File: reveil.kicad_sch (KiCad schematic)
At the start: 18 parts, among them J1 Barrel_Jack_Switch, J2 AudioJack3_SwitchTR, M1 Motor_DC, Q1 2N3904, Q2 IRF540N

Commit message: Corrige le pinout du footprint du switch ALARME_ON_OFF1 (court-circuit GND/+3V3)
Le footprint système Button_Switch_THT:SW_Slide-03_Wuerth-WS-SLTV a
les pads 1 et 2 physiquement inversés par rapport au composant monté
(pin 1 attendu à gauche, pin 2 au centre — le footprint avait
l'inverse). Résultat : selon la position du switch, +3V3 et GND se
retrouvaient court-circuités via l'interrupteur, faisant chauffer le
Pico et les câbles d'alimentation.

Correctif : nouvelle librairie locale reveil.pretty/ avec une copie
du footprint où seuls les pads 1 et 2 échangent leur géométrie (même
taille/forme/perçage, juste la position), enregistrée via
fp-lib-table. Le schéma (ALARME_ON_OFF1) et le PCB référencent
maintenant reveil:SW_Slide-03_... ; les pistes ont été reroutées en
conséquence.

Confirmé par :
- Mesure au multimètre (court quasi 0 Ω entre GND et +3V3, reproduit
  en rebranchant ces deux fils) ayant permis d'identifier la cause
- ERC propre (0 erreur/avertissement)
- DRC propre après routage (plus de shorting_items ni de pad non
  connecté sur ALARME_ON_OFF1)

Co-Authored-By: Claude Sonnet 5 <noreply@anthropic.com>
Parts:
- ALARME_ON_OFF1: footprint Button_Switch_THT:SW_Slide-03_Wuerth-WS-SLTV_10x2.5x6.4_P2.54mm -> reveil:SW_Slide-03_Wuerth-WS-SLTV_10x2.5x6.4_P2.54mm
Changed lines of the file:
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@@
 			)
 		)
-		(property "Footprint" "Button_Switch_THT:SW_Slide-03_Wuerth-WS-SLTV_10x2.5x6.4_P2.54mm"
+		(property "Footprint" "reveil:SW_Slide-03_Wuerth-WS-SLTV_10x2.5x6.4_P2.54mm"
 			(at 91.44 144.78 0)
 			(effects

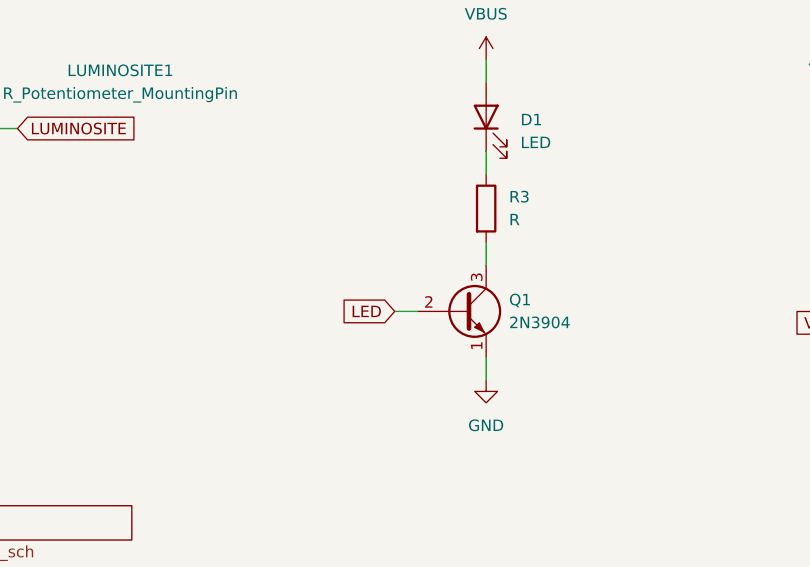
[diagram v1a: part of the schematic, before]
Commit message: Ajoute R4 (résistance de base) et corrige R3 pour le circuit LED D1
GP17 pilotait directement la base de Q1 sans résistance série : la
broche ne pouvait pas atteindre un état haut propre (chargée par la
jonction base-émetteur, ~0.6-0.7V), maintenant Q1 en conduction
partielle constante au lieu de commuter — la LED restait allumée en
continu, faiblement, au lieu de clignoter.

- R4 = 1.5 kΩ ajoutée en série entre GP17 et la base de Q1
  (Ib ≈ 1.73 mA pour Ic ≈ 16 mA, marge confortable vs hFE_min du
  2N3904 pour garantir la saturation)
- R3 = 100 Ω (au lieu de 47K, qui aurait donné ~34 µA, LED quasi
  éteinte) pour ~16 mA dans D1 (LED blanche, Vf≈3.2V supposé),
  environ 20% sous le courant max typique d'une LED THT 3mm générique

Vérifié par ERC (0 erreur/avertissement). Placement PCB et routage
de R4 restent à faire.

Co-Authored-By: Claude Sonnet 5 <noreply@anthropic.com>
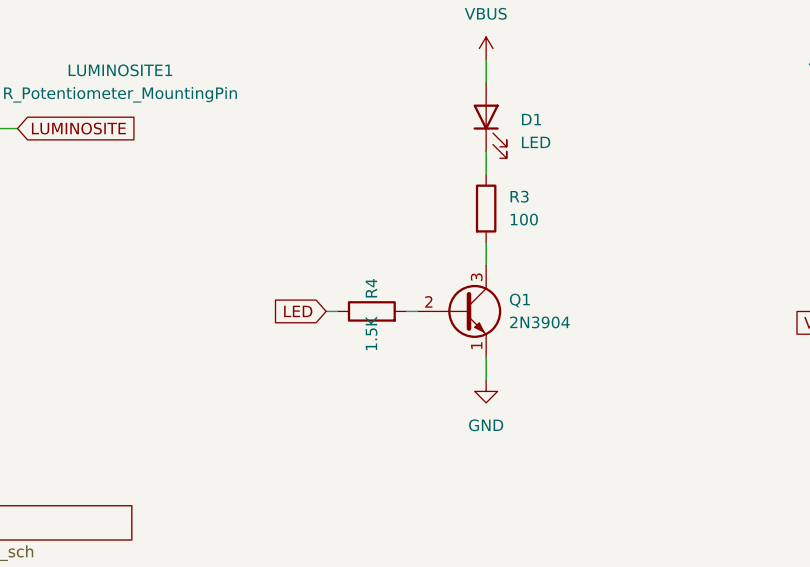
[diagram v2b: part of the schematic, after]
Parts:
- added R4: 1.5K, Resistor_THT:R_Axial_DIN0207_L6.3mm_D2.5mm_P7.62mm_Horizontal, symbol Device:R
- R3: value R -> 100
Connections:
- net LED: now also R4.1; no longer Q1.2 (B)
- new net: Q1.2 (B), R4.2
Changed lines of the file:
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@@
 	(wire
 		(pts
-			(xy 184.15 143.51) (xy 186.69 143.51)
-		)
-		(stroke
-			(width 0)
-			(type default)
+			(xy 176.53 143.51) (xy 177.8 143.51)
+		)
+		(stroke
+			(width 0)
+			(type default)
+		)
+	)
+	(wire
+		(pts
+			(xy 185.42 143.51) (xy 186.69 143.51)
+		)
+		(stroke
+			(width 0)
+			(type default)
+		)
+	)
+	(symbol
+		(lib_id "Device:R")
+		(at 181.61 143.51 90)
+		(unit 1)
+		(exclude_from_sim no)
+		(in_bom yes)
+		(on_board yes)
+		(dnp no)
+		(fields_autoplaced yes)
+		(property "Reference" "R4"
+			(at 181.61 140.97 0)
+			(effects
+				(font
+					(size 1.27 1.27)
+				)
+			)
+		)
+		(property "Value" "1.5K"
+			(at 181.61 146.05 0)
+			(effects
+				(font
+					(size 1.27 1.27)
+				)
+			)
+		)
+		(property "Footprint" "Resistor_THT:R_Axial_DIN0207_L6.3mm_D2.5mm_P7.62mm_Horizontal"
+			(at 181.61 143.51 0)
+			(effects
+				(font
+					(size 1.27 1.27)
+				)
+				(hide yes)
+			)
+		)
+		(property "Datasheet" "~"
+			(at 181.61 143.51 0)
+			(effects
+				(font
+					(size 1.27 1.27)
+				)
+				(hide yes)
+			)
+		)
+		(property "Description" "Resistor"
+			(at 181.61 143.51 0)
+			(effects
+				(font
+					(size 1.27 1.27)
+				)
+				(hide yes)
+			)
+		)
+		(pin "1"
+		)
+		(pin "2"
+		)
+		(instances
+			(project ""
+				(path "/6015885c-867c-4e88-9a3e-de8167bfed74"
+					(reference "R4")
+					(unit 1)
+				)
+			)
 		)
 	)
@@
 	(global_label "LED"
 		(shape input)
-		(at 184.15 143.51 180)
-		(fields_autoplaced yes)
-		(effects
-			(font
-				(size 1.27 1.27)
-			)
-			(justify right)
-		)
-		(property "Intersheetrefs" "${INTERSHEET_REFS}"
-			(at 177.7177 143.51 0)
+		(at 176.53 143.51 180)
+		(fields_autoplaced yes)
+		(effects
+			(font
+				(size 1.27 1.27)
+			)
+			(justify right)
+		)
+		(property "Intersheetrefs" "${INTERSHEET_REFS}"
+			(at 170.0977 143.51 0)
 			(effects
 				(font
@@
 			)
 		)
-		(property "Value" "R"
+		(property "Value" "100"
 			(at 196.85 133.3499 0)
 			(effects

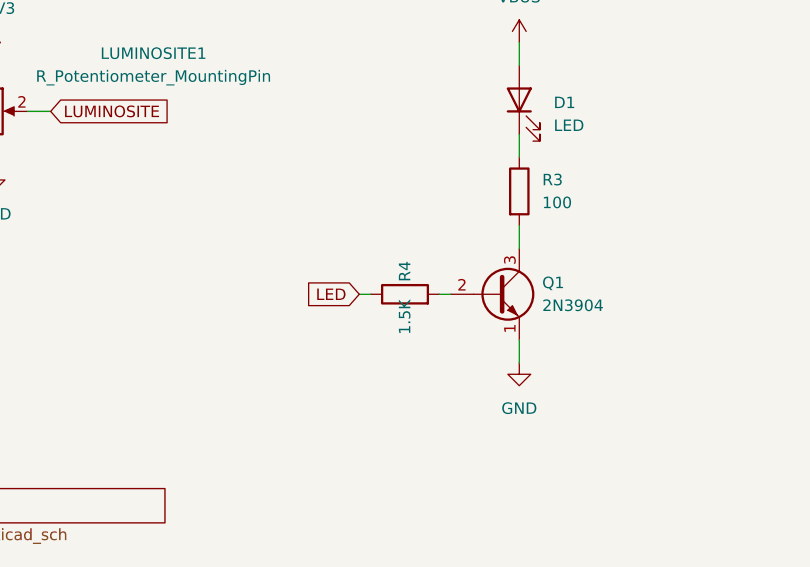
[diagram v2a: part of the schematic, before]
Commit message: Place et route R4 sur le PCB (résistance de base LED)
R4 (1.5 kΩ, ajoutée au schéma dans le commit précédent) est
maintenant placée et routée sur le PCB. reveil.kicad_sch est
reformaté par KiCad (réordonnancement interne des blocs, aucun
changement électrique) suite à la synchronisation schéma/PCB.

Vérifié par ERC (0 erreur/avertissement) et DRC (0 pad non connecté,
0 erreur de footprint ; seuls restent des avertissements
silk_edge_clearance préexistants sur J2, sans rapport avec ce fix).

Test fonctionnel de la LED pas encore fait : une correction PCB
supplémentaire est nécessaire avant de pouvoir tester (voir TODO
README).

Co-Authored-By: Claude Sonnet 5 <noreply@anthropic.com>
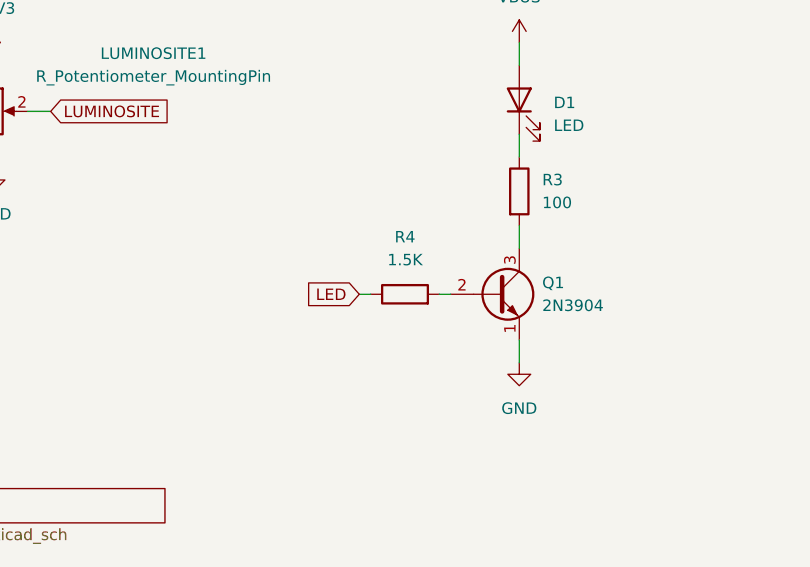
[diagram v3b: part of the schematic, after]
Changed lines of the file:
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@@
 	(wire
 		(pts
+			(xy 176.53 143.51) (xy 177.8 143.51)
+		)
+		(stroke
+			(width 0)
+			(type default)
+		)
+	)
+	(wire
+		(pts
 			(xy 99.06 147.32) (xy 99.06 149.86)
 		)
@@
 	(wire
 		(pts
-			(xy 176.53 143.51) (xy 177.8 143.51)
-		)
-		(stroke
-			(width 0)
-			(type default)
-		)
-	)
-	(wire
-		(pts
-			(xy 185.42 143.51) (xy 186.69 143.51)
-		)
-		(stroke
-			(width 0)
-			(type default)
-		)
-	)
-	(symbol
-		(lib_id "Device:R")
-		(at 181.61 143.51 90)
-		(unit 1)
-		(exclude_from_sim no)
-		(in_bom yes)
-		(on_board yes)
-		(dnp no)
-		(fields_autoplaced yes)
-		(property "Reference" "R4"
-			(at 181.61 140.97 0)
-			(effects
-				(font
-					(size 1.27 1.27)
-				)
-			)
-		)
-		(property "Value" "1.5K"
-			(at 181.61 146.05 0)
-			(effects
-				(font
-					(size 1.27 1.27)
-				)
-			)
-		)
-		(property "Footprint" "Resistor_THT:R_Axial_DIN0207_L6.3mm_D2.5mm_P7.62mm_Horizontal"
-			(at 181.61 143.51 0)
-			(effects
-				(font
-					(size 1.27 1.27)
-				)
-				(hide yes)
-			)
-		)
-		(property "Datasheet" "~"
-			(at 181.61 143.51 0)
-			(effects
-				(font
-					(size 1.27 1.27)
-				)
-				(hide yes)
-			)
-		)
-		(property "Description" "Resistor"
-			(at 181.61 143.51 0)
-			(effects
-				(font
-					(size 1.27 1.27)
-				)
-				(hide yes)
-			)
-		)
-		(pin "1"
-		)
-		(pin "2"
-		)
-		(instances
-			(project ""
-				(path "/6015885c-867c-4e88-9a3e-de8167bfed74"
-					(reference "R4")
-					(unit 1)
-				)
-			)
-		)
-	)
-	(wire
-		(pts
 			(xy 246.38 76.2) (xy 246.38 77.47)
 		)
@@
 	(wire
 		(pts
+			(xy 185.42 143.51) (xy 186.69 143.51)
+		)
+		(stroke
+			(width 0)
+			(type default)
+		)
+	)
+	(wire
+		(pts
 			(xy 57.15 68.58) (xy 59.69 68.58)
 		)
@@
 					(unit 1)
 				)
+			)
+		)
+	)
+	(symbol
+		(lib_id "Device:R")
+		(at 181.61 143.51 90)
+		(unit 1)
+		(exclude_from_sim no)
+		(in_bom yes)
+		(on_board yes)
+		(dnp no)
+		(fields_autoplaced yes)
+		(property "Reference" "R4"
+			(at 181.61 137.16 90)
+			(effects
+				(font
+					(size 1.27 1.27)
+				)
+			)
+		)
+		(property "Value" "1.5K"
+			(at 181.61 139.7 90)
+			(effects
+				(font
+					(size 1.27 1.27)
+				)
+			)
+		)
+		(property "Footprint" "Resistor_THT:R_Axial_DIN0207_L6.3mm_D2.5mm_P7.62mm_Horizontal"
+			(at 181.61 145.288 90)
+			(effects
+				(font
+					(size 1.27 1.27)
+				)
+				(hide yes)
+			)
+		)
+		(property "Datasheet" "~"
+			(at 181.61 143.51 0)
+			(effects
+				(font
+					(size 1.27 1.27)
+				)
+				(hide yes)
+			)
+		)
+		(property "Description" "Resistor"
+			(at 181.61 143.51 0)
+			(effects
+				(font
+					(size 1.27 1.27)
+				)
+				(hide yes)
+			)
+		)
+		(pin "2"
+		)
+		(pin "1"
+		)
+		(instances
+			(project "reveil"
+				(path "/6015885c-867c-4e88-9a3e-de8167bfed74"
+					(reference "R4")
+					(unit 1)
+				)

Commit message: Remplace Q2 (IRF510/IRF540N) par un IRLB8721PbF logic-level et ajoute R5
Le RP2040 pilote la grille de Q2 directement en 3.3V (GP18), et ni
l'IRF510 (carte physique) ni l'IRF540N (schéma) ne sont des MOSFET
logic-level (Rds(on) specifie a Vgs=10V) : risque de sous-enhancement
et d'echauffement. L'IRLB8721PbF est pleinement enhance des 2.5-4.5V,
compatible avec un pilotage direct en 3.3V.

Ajoute R5 = 100 ohm en serie entre GP18 et la grille de Q2 pour
limiter le pic de courant transitoire et amortir le ringing.

Verifie : pinout G/D/S (broches 1/2/3, meme convention que l'IRF540N),
footprint TO-220-3_Horizontal_TabDown (corrige apres reperage d'un
TO-220F errone), ERC (0 violation) et DRC (6 avertissements
preexistants sur J2, sans rapport).

Co-Authored-By: Claude Sonnet 5 <noreply@anthropic.com>
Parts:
- removed Q2: IRF540N, Package_TO_SOT_THT:TO-220-3_Horizontal_TabDown, symbol Transistor_FET:IRF540N
- added Q2: IRLB8721PBF, Package_TO_SOT_THT:TO-220-3_Horizontal_TabDown, symbol Transistor_FET:IRLB8721PBF
- added R5: 100R, Resistor_THT:R_Axial_DIN0207_L6.3mm_D2.5mm_P7.62mm_Horizontal, symbol Device:R
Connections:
- net GND: now also Q2.3 (S)
- net VIBREUR: now also R5.1
- net at J2.T, M1.2 (-): now also Q2.2 (D)
- new net: Q2.1 (G), R5.2
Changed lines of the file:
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@@
 	(wire
 		(pts
+			(xy 228.6 144.78) (xy 231.14 144.78)
+		)
+		(stroke
+			(width 0)
+			(type default)
+		)
+	)
+	(wire
+		(pts
 			(xy 167.64 38.1) (xy 167.64 46.99)
 		)
@@
 	(wire
 		(pts
+			(xy 238.76 144.78) (xy 241.3 144.78)
+		)
+		(stroke
+			(width 0)
+			(type default)
+		)
+	)
+	(wire
+		(pts
 			(xy 246.38 76.2) (xy 246.38 77.47)
 		)
@@
 	(wire
 		(pts
-			(xy 238.76 144.78) (xy 241.3 144.78)
-		)
-		(stroke
-			(width 0)
-			(type default)
-		)
-	)
-	(wire
-		(pts
 			(xy 57.15 48.26) (xy 59.69 48.26)
 		)
@@
 	(global_label "VIBREUR"
 		(shape input)
-		(at 238.76 144.78 180)
+		(at 228.6 144.78 180)
 		(fields_autoplaced yes)
 		(effects
@@
 		)
 		(property "Intersheetrefs" "${INTERSHEET_REFS}"
-			(at 227.7919 144.78 0)
+			(at 217.6319 144.78 0)
 			(effects
 				(font
@@
 	)
 	(symbol
+		(lib_id "Transistor_FET:IRLB8721PBF")
+		(at 246.38 144.78 0)
+		(unit 1)
+		(exclude_from_sim no)
+		(in_bom yes)
+		(on_board yes)
+		(dnp no)
+		(fields_autoplaced yes)
+		(property "Reference" "Q2"
+			(at 252.73 143.5099 0)
+			(effects
+				(font
+					(size 1.27 1.27)
+				)
+				(justify left)
+			)
+		)
+		(property "Value" "IRLB8721PBF"
+			(at 252.73 146.0499 0)
+			(effects
+				(font
+					(size 1.27 1.27)
+				)
+				(justify left)
+			)
+		)
+		(property "Footprint" "Package_TO_SOT_THT:TO-220-3_Horizontal_TabDown"
+			(at 251.46 146.685 0)
+			(effects
+				(font
+					(size 1.27 1.27)
+					(italic yes)
+				)
+				(justify left)
+				(hide yes)
+			)
+		)
+		(property "Datasheet" "http://www.infineon.com/dgdl/irlb8721pbf.pdf?fileId=5546d462533600a40153566056732591"
+			(at 251.46 148.59 0)
+			(effects
+				(font
+					(size 1.27 1.27)
+				)
+				(justify left)
+				(hide yes)
+			)
+		)
+		(property "Description" "62A Id, 30V Vds, 8.7 mOhm Rds, N-Channel HEXFET Power MOSFET, TO-220"
+			(at 246.38 144.78 0)
+			(effects
+				(font
+					(size 1.27 1.27)
+				)
+				(hide yes)
+			)
+		)
+		(pin "3"
+		)
+		(pin "2"
+		)
+		(pin "1"
+		)
+		(instances
+			(project ""
+				(path "/6015885c-867c-4e88-9a3e-de8167bfed74"
+					(reference "Q2")
+					(unit 1)
+				)
+			)
+		)
+	)
+	(symbol
 		(lib_id "power:GND")
 		(at 99.06 149.86 0)
@@
 	)
 	(symbol
-		(lib_id "Transistor_FET:IRF540N")
-		(at 246.38 144.78 0)
-		(unit 1)
-		(exclude_from_sim no)
-		(in_bom yes)
-		(on_board yes)
-		(dnp no)
-		(fields_autoplaced yes)
-		(property "Reference" "Q2"
-			(at 252.73 143.5099 0)
-			(effects
-				(font
-					(size 1.27 1.27)
-				)
-				(justify left)
-			)
-		)
-		(property "Value" "IRF540N"
-			(at 252.73 146.0499 0)
-			(effects
-				(font
-					(size 1.27 1.27)
-				)
-				(justify left)
-			)
-		)
-		(property "Footprint" "Package_TO_SOT_THT:TO-220-3_Horizontal_TabDown"
-			(at 251.46 146.685 0)
-			(effects
-				(font
-					(size 1.27 1.27)
-					(italic yes)
-				)
-				(justify left)
-				(hide yes)
-			)
-		)
-		(property "Datasheet" "http://www.irf.com/product-info/datasheets/data/irf540n.pdf"
-			(at 251.46 148.59 0)
-			(effects
-				(font
-					(size 1.27 1.27)
-				)
-				(justify left)
-				(hide yes)
-			)
-		)
-		(property "Description" "33A Id, 100V Vds, HEXFET N-Channel MOSFET, TO-220"
-			(at 246.38 144.78 0)
-			(effects
-				(font
-					(size 1.27 1.27)
-				)
-				(hide yes)
-			)
-		)
-		(pin "3"
-		)
-		(pin "2"
-		)
-		(pin "1"
-		)
-		(instances
-			(project ""
-				(path "/6015885c-867c-4e88-9a3e-de8167bfed74"
-					(reference "Q2")
-					(unit 1)
-				)
-			)
-		)
-	)
-	(symbol
 		(lib_id "power:+3V3")
 		(at 135.89 116.84 0)
@@
 					(unit 1)
 				)
+			)
+		)
+	)
+	(symbol
+		(lib_id "Device:R")
+		(at 234.95 144.78 90)
+		(unit 1)
+		(exclude_from_sim no)
+		(in_bom yes)
+		(on_board yes)
+		(dnp no)
+		(fields_autoplaced yes)
+		(property "Reference" "R5"
+			(at 234.95 138.43 90)
+			(effects
+				(font
+					(size 1.27 1.27)
+				)
+			)
+		)
+		(property "Value" "100R"
+			(at 234.95 140.97 90)
+			(effects
+				(font
+					(size 1.27 1.27)
+				)
+			)
+		)
+		(property "Footprint" "Resistor_THT:R_Axial_DIN0207_L6.3mm_D2.5mm_P7.62mm_Horizontal"
+			(at 234.95 146.558 90)
+			(effects
+				(font
+					(size 1.27 1.27)
+				)
+				(hide yes)
+			)
+		)
+		(property "Datasheet" "~"
+			(at 234.95 144.78 0)
+			(effects
+				(font
+					(size 1.27 1.27)
+				)
+				(hide yes)
+			)
+		)
+		(property "Description" "Resistor"
+			(at 234.95 144.78 0)
+			(effects
+				(font
+					(size 1.27 1.27)
+				)
+				(hide yes)
+			)
+		)
+		(pin "2"
+		)
+		(pin "1"
+		)
+		(instances
+			(project "reveil"
+				(path "/6015885c-867c-4e88-9a3e-de8167bfed74"
+					(reference "R5")
+					(unit 1)
+				)

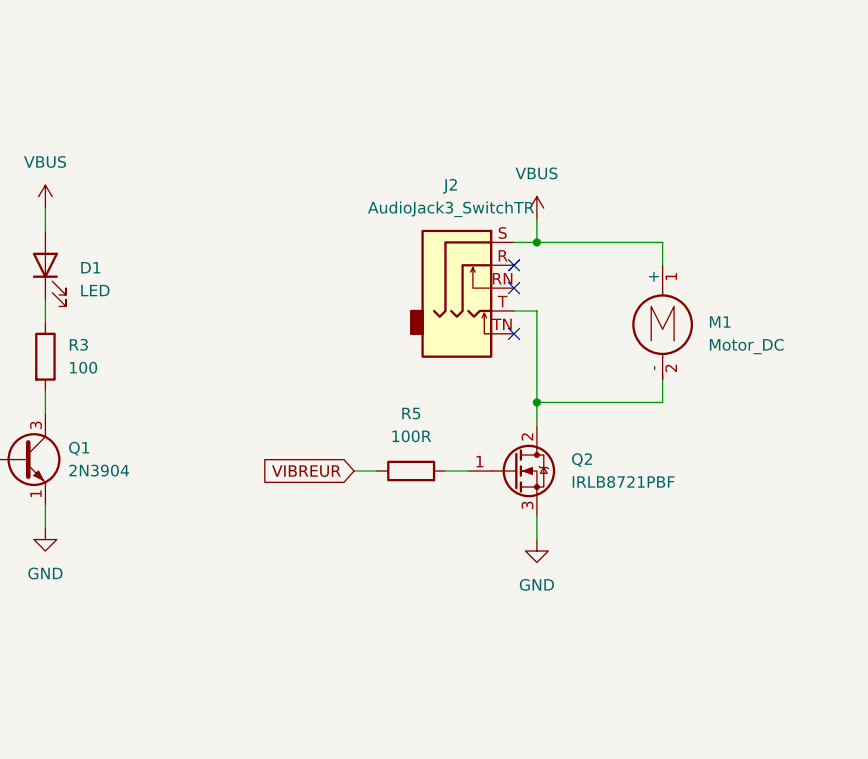
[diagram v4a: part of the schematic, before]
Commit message: Schéma/PCB : ajoute la diode de roue libre et le snubber du moteur
Rien ne protégeait le drain de Q2 contre la surtension inductive à la
coupure du moteur M1 (roue libre) : l'avalanche de Q2 absorbait
l'énergie et parasitait le 5 V du Pico.

Ajoute en parallèle de M1, entre le drain de Q2 et VBUS :
- D2 (Schottky 1N5819), cathode côté VBUS, anode côté drain de Q2
- C5 (100 nF) contre les parasites de commutation des balais du moteur

Empreintes placées et pistes routées sur le PCB ; schéma réorganisé
pour la lisibilité.

Connectivité vérifiée via le netlist KiCad (D2 cathode sur le net VBUS,
D2 anode + C5 sur le même net que le drain de Q2 / M1) et ERC/DRC
revérifiés via le conteneur Docker KiBot : 0 erreur/avertissement ERC ;
DRC revenu à la référence (6 avertissements silk_edge_clearance
préexistants sur J2), aucun écart schéma/PCB.

Co-Authored-By: Claude Sonnet 5 <noreply@anthropic.com>
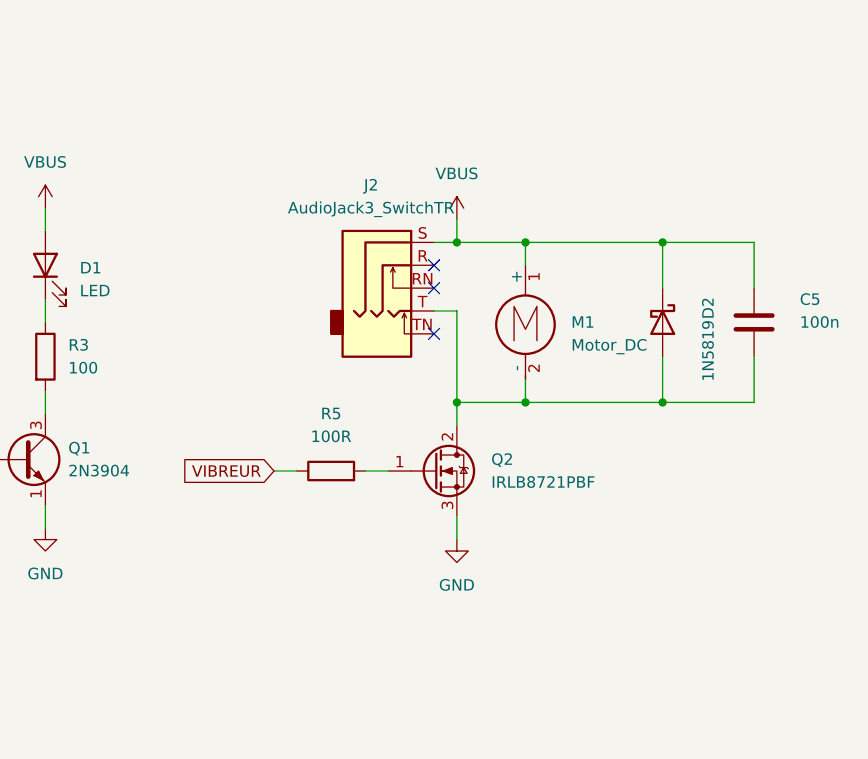
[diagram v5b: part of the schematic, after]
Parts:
- added C5: 100n, Capacitor_THT:C_Disc_D3.0mm_W1.6mm_P2.50mm, symbol Device:C
- added D2: 1N5819, Diode_THT:D_DO-41_SOD81_P10.16mm_Horizontal, symbol Device:D_Schottky
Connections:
- net VBUS: now also C5.1, D2.1 (K)
- net at J2.T, M1.2 (-), Q2.2 (D): now also C5.2, D2.2 (A)
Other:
- moved on the sheet: J2, M1, Q2, R5
